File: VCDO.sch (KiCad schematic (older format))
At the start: 84 parts, among them J1 PCB INTERCONNECT, J2 PROGRAMMING HEADER, Q1 2N3904, U1 TL074, U2 Druid VCDO, U3 TL074, U4 TL072

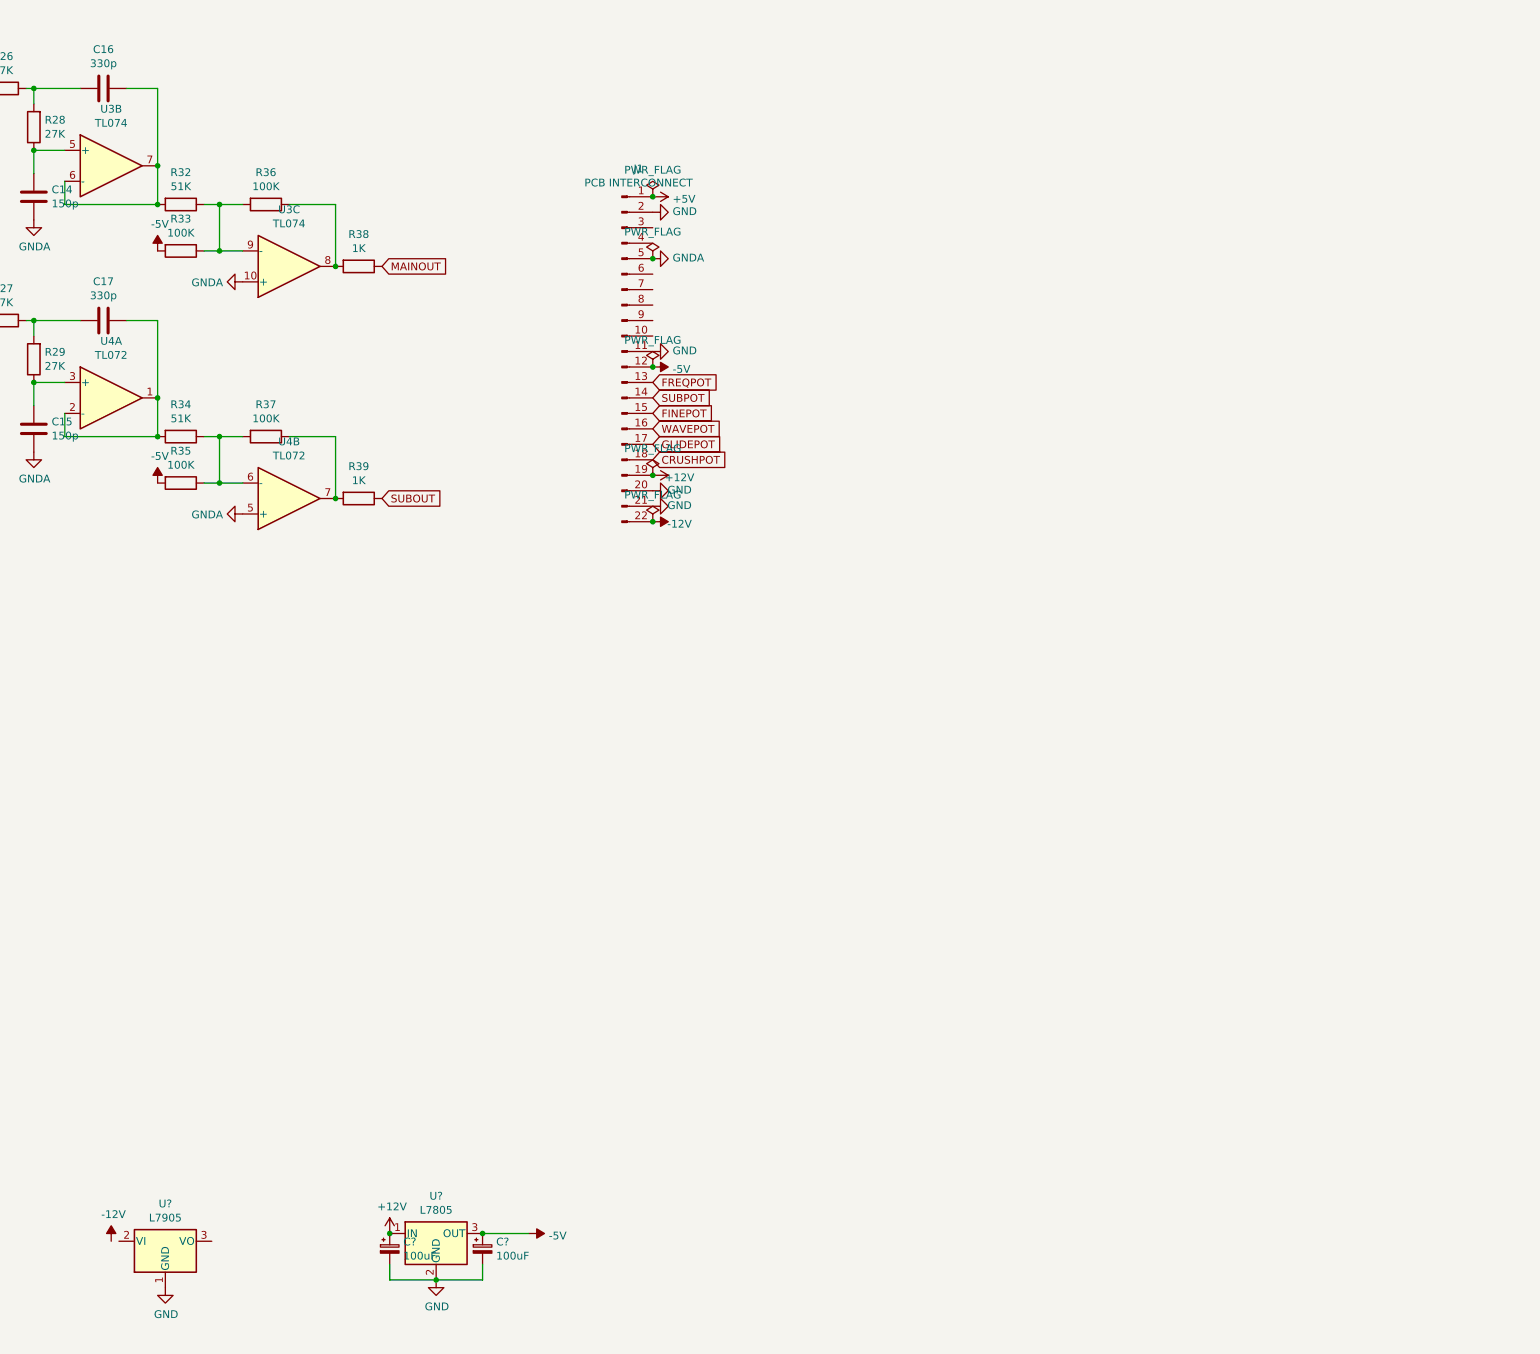
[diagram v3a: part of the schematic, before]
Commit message: no more conn, add pots
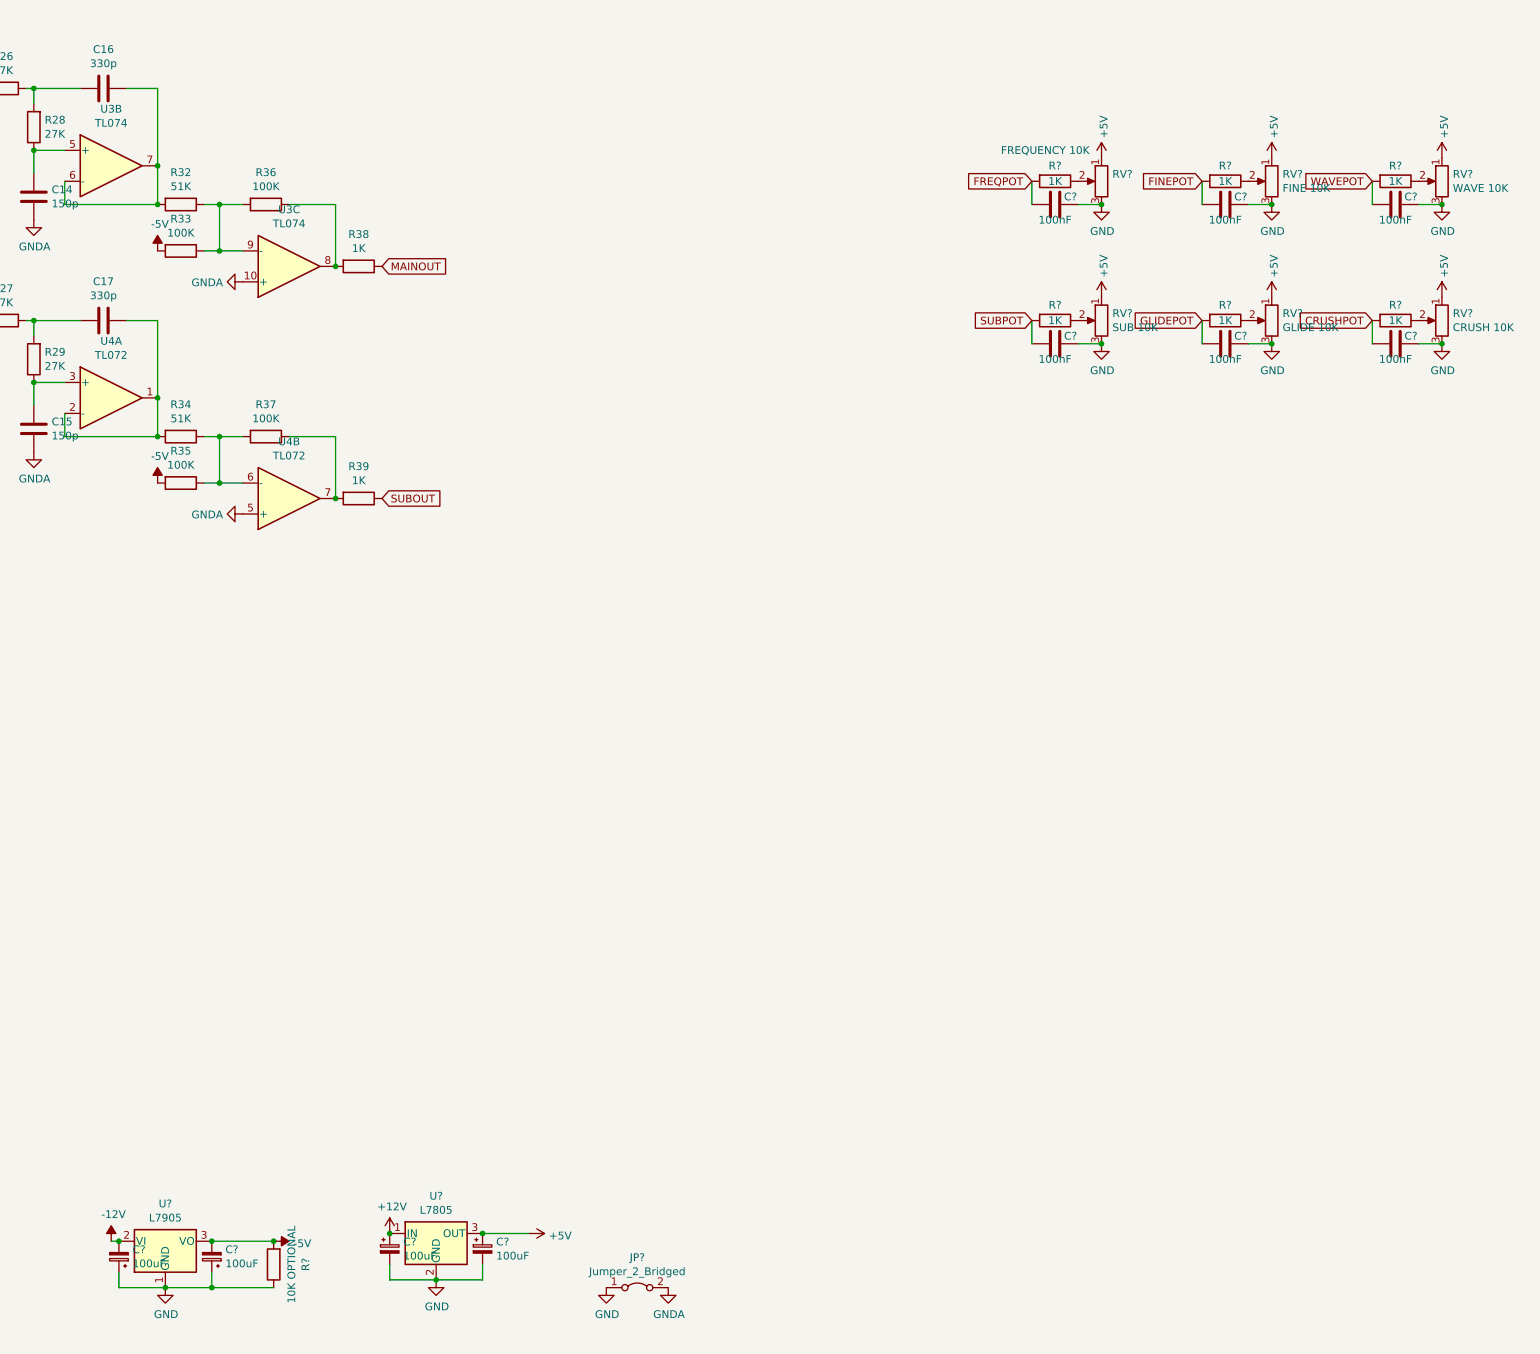
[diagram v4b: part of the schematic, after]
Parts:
- removed J1: PCB INTERCONNECT, Connector_PinHeader_2.54mm:PinHeader_1x22_P2.54mm_Vertical, symbol Connector:Conn_01x22_Male
- added C? (x2): 100uF, symbol Device:CP_Small
- added C? (x6): 100nF, symbol Device:C
- added JP?: Jumper_2_Bridged, symbol Jumper:Jumper_2_Bridged
- added R?: 10K OPTIONAL, Resistor_THT:R_Axial_DIN0207_L6.3mm_D2.5mm_P7.62mm_Horizontal, symbol Device:R
- added R? (x6): 1K, Resistor_THT:R_Axial_DIN0207_L6.3mm_D2.5mm_P7.62mm_Horizontal, symbol Device:R
- added RV?: FREQUENCY 10K, symbol Device:R_POT
- added RV?: FINE 10K, symbol Device:R_POT
- added RV?: WAVE 10K, symbol Device:R_POT
- added RV?: SUB 10K, symbol Device:R_POT
- added RV?: GLIDE 10K, symbol Device:R_POT
- added RV?: CRUSH 10K, symbol Device:R_POT
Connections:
- net +5V: now also C?.1, U?.3 (OUT), RV?.1, RV?.1, RV?.1, RV?.1, RV?.1, RV?.1
- net -12V: now also U?.2 (VI), C?.2
- net -5V: now also U?.3 (VO), C?.2, R?.2; no longer C?.1, U?.3 (OUT)
- net CRUSHPOT: now also C?.2, R?.2
- net FINEPOT: now also C?.2, R?.2
- net FREQPOT: now also C?.2, R?.2
- net GLIDEPOT: now also C?.2, R?.2
- net GND: now also C?.1, C?.1, C?.1, C?.1, C?.1, C?.1, C?.1, C?.1, JP?.1 (A), R?.1, RV?.3, RV?.3, RV?.3, RV?.3, RV?.3, RV?.3
- net GNDA: now also JP?.2 (B)
- net SUBPOT: now also C?.2, R?.2
- net WAVEPOT: now also C?.2, R?.2
- new net: R?.1, RV?.2 (x6)

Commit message: reannotate
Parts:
- gave numbers to parts that had none: 38
- renumbered C2 to C1, C11 to C10, C14 to C11, C15 to C12, C16 to C13, C17 to C14, C1 to C18, C3 to C2, C4 to C3, C5 to C4, C6 to C5, C7 to C6, C8 to C7, C9 to C8, C10 to C9, J2 to J10, R20 to R18, R21 to R19, R18 to R20, R22 to R21, R23 to R22, R26 to R23, R27 to R24, R28 to R25, R29 to R26, R32 to R27, R33 to R28, R34 to R29, R35 to R30, R36 to R31, R37 to R32, R38 to R34, R39 to R35, R19 to R36, RV1 to RV4, RV2 to RV5, RV3 to RV6, U3 to U2, U4 to U3, U2 to U6

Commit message: pwr flags
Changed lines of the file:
@@
 Wire Wire Line
 	14750 4600 14750 4750
+$Comp
+L power:PWR_FLAG #FLG0101
+U 1 1 60C07709
+P 4500 10000
+F 0 "#FLG0101" H 4500 10075 50  0001 C CNN
+F 1 "PWR_FLAG" H 4500 10173 50  0000 C CNN
+F 2 "" H 4500 10000 50  0001 C CNN
+F 3 "~" H 4500 10000 50  0001 C CNN
+	1    4500 10000
+	1    0    0    -1
+$EndComp
+Connection ~ 4500 10000
+$Comp
+L power:PWR_FLAG #FLG0102
+U 1 1 60C07B37
+P 4600 10400
+F 0 "#FLG0102" H 4600 10475 50  0001 C CNN
+F 1 "PWR_FLAG" H 4600 10573 50  0000 C CNN
+F 2 "" H 4600 10400 50  0001 C CNN
+F 3 "~" H 4600 10400 50  0001 C CNN
+	1    4600 10400
+	1    0    0    -1
+$EndComp
+Connection ~ 4600 10400
+$Comp
+L power:PWR_FLAG #FLG0103
+U 1 1 60C07EDA
+P 4000 10700
+F 0 "#FLG0103" H 4000 10775 50  0001 C CNN
+F 1 "PWR_FLAG" V 4000 10827 50  0000 L CNN
+F 2 "" H 4000 10700 50  0001 C CNN
+F 3 "~" H 4000 10700 50  0001 C CNN
+	1    4000 10700
+	0    -1   -1   0
+$EndComp
+Connection ~ 4000 10700
 $EndSCHEMATC

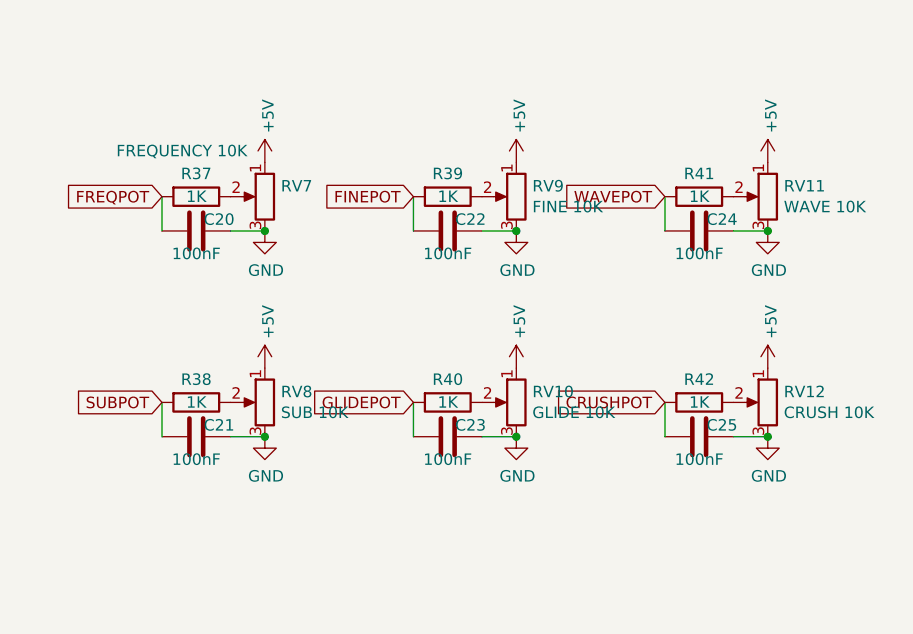
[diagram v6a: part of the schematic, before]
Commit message: no more resistors or caps on pots
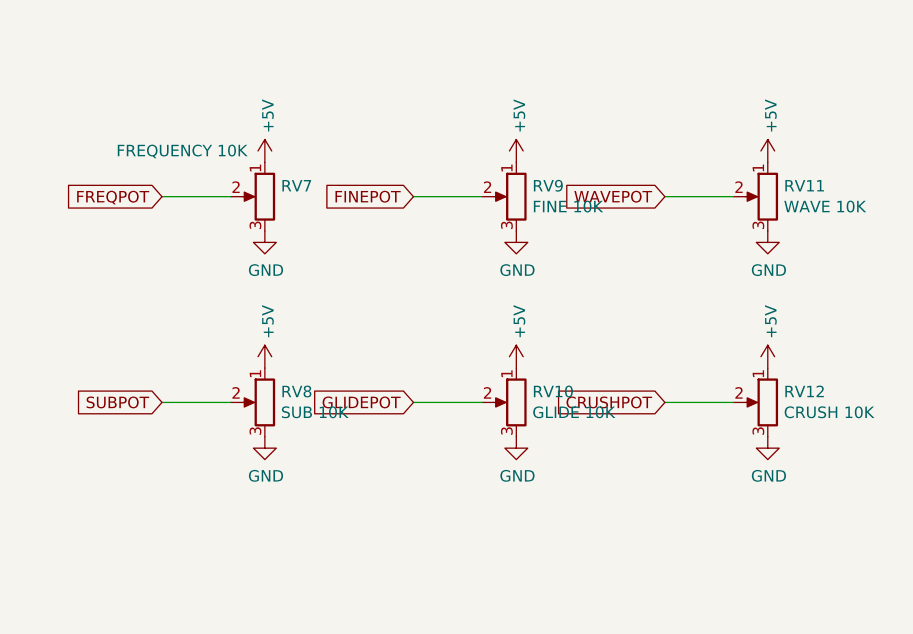
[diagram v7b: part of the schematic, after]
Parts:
- removed C20, C21, C22, C23, C24, C25: 100nF, symbol Device:C
- removed R37, R38, R39, R40, R41, R42: 1K, Resistor_THT:R_Axial_DIN0207_L6.3mm_D2.5mm_P7.62mm_Horizontal, symbol Device:R
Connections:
- net CRUSHPOT: now also RV12.2
- net FINEPOT: now also RV9.2
- net FREQPOT: now also RV7.2
- net GLIDEPOT: now also RV10.2
- net SUBPOT: now also RV8.2
- net WAVEPOT: now also RV11.2
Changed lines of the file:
@@
-$EndComp
-$Comp
-L Device:R R37
-U 1 1 60C8DA64
-P 12700 3700
-F 0 "R37" V 12600 3700 50  0000 C CNN
-F 1 "1K" V 12700 3700 50  0000 C CNN
-F 2 "Resistor_THT:R_Axial_DIN0207_L6.3mm_D2.5mm_P7.62mm_Horizontal" V 12630 3700 50  0001 C CNN
-F 3 "~" H 12700 3700 50  0001 C CNN
-	1    12700 3700
-	0    1    1    0
-$EndComp
-$Comp
-L Device:C C20
-U 1 1 60C945AD
-P 12700 3850
-F 0 "C20" V 12650 3950 50  0000 C CNN
-F 1 "100nF" V 12800 3850 50  0000 C CNN
-F 2 "" H 12738 3700 50  0001 C CNN
-F 3 "~" H 12700 3850 50  0001 C CNN
-	1    12700 3850
-	0    1    1    0
 $EndComp
 $Comp
@@
 	1    0    0    -1
 $EndComp
-Wire Wire Line
-	12850 3850 13000 3850
-Connection ~ 13000 3850
-Wire Wire Line
-	12550 3700 12550 3850
 $Comp
 L Device:R_POT RV9
@@
 $EndComp
 $Comp
-L Device:R R39
-U 1 1 60CA3A2C
-P 13800 3700
-F 0 "R39" V 13700 3700 50  0000 C CNN
-F 1 "1K" V 13800 3700 50  0000 C CNN
-F 2 "Resistor_THT:R_Axial_DIN0207_L6.3mm_D2.5mm_P7.62mm_Horizontal" V 13730 3700 50  0001 C CNN
-F 3 "~" H 13800 3700 50  0001 C CNN
-	1    13800 3700
-	0    1    1    0
-$EndComp
-$Comp
-L Device:C C22
-U 1 1 60CA3A36
-P 13800 3850
-F 0 "C22" V 13750 3950 50  0000 C CNN
-F 1 "100nF" V 13900 3850 50  0000 C CNN
-F 2 "" H 13838 3700 50  0001 C CNN
-F 3 "~" H 13800 3850 50  0001 C CNN
-	1    13800 3850
-	0    1    1    0
-$EndComp
-$Comp
 L power:+5V #PWR074
 U 1 1 60CA3A40
@@
 	1    0    0    -1
 $EndComp
-Wire Wire Line
-	13950 3850 14100 3850
-Connection ~ 14100 3850
-Wire Wire Line
-	13650 3700 13650 3850
 $Comp
 L Device:R_POT RV11
@@
 $EndComp
 $Comp
-L Device:R R41
-U 1 1 60CAB3F1
-P 14900 3700
-F 0 "R41" V 14800 3700 50  0000 C CNN
-F 1 "1K" V 14900 3700 50  0000 C CNN
-F 2 "Resistor_THT:R_Axial_DIN0207_L6.3mm_D2.5mm_P7.62mm_Horizontal" V 14830 3700 50  0001 C CNN
-F 3 "~" H 14900 3700 50  0001 C CNN
-	1    14900 3700
-	0    1    1    0
-$EndComp
-$Comp
-L Device:C C24
-U 1 1 60CAB3FB
-P 14900 3850
-F 0 "C24" V 14850 3950 50  0000 C CNN
-F 1 "100nF" V 15000 3850 50  0000 C CNN
-F 2 "" H 14938 3700 50  0001 C CNN
-F 3 "~" H 14900 3850 50  0001 C CNN
-	1    14900 3850
-	0    1    1    0
-$EndComp
-$Comp
 L power:+5V #PWR078
 U 1 1 60CAB405
@@
 	1    0    0    -1
 $EndComp
-Wire Wire Line
-	15050 3850 15200 3850
-Connection ~ 15200 3850
-Wire Wire Line
-	14750 3700 14750 3850
 $Comp
 L Device:R_POT RV8
@@
 $EndComp
 $Comp
-L Device:R R38
-U 1 1 60CB31F0
-P 12700 4600
-F 0 "R38" V 12600 4600 50  0000 C CNN
-F 1 "1K" V 12700 4600 50  0000 C CNN
-F 2 "Resistor_THT:R_Axial_DIN0207_L6.3mm_D2.5mm_P7.62mm_Horizontal" V 12630 4600 50  0001 C CNN
-F 3 "~" H 12700 4600 50  0001 C CNN
-	1    12700 4600
-	0    1    1    0
-$EndComp
-$Comp
-L Device:C C21
-U 1 1 60CB31FA
-P 12700 4750
-F 0 "C21" V 12650 4850 50  0000 C CNN
-F 1 "100nF" V 12800 4750 50  0000 C CNN
-F 2 "" H 12738 4600 50  0001 C CNN
-F 3 "~" H 12700 4750 50  0001 C CNN
-	1    12700 4750
-	0    1    1    0
-$EndComp
-$Comp
 L power:+5V #PWR072
 U 1 1 60CB3204
@@
 	1    0    0    -1
 $EndComp
-Wire Wire Line
-	12850 4750 13000 4750
-Connection ~ 13000 4750
-Wire Wire Line
-	12550 4600 12550 4750
 $Comp
 L Device:R_POT RV10
@@
 $EndComp
 $Comp
-L Device:R R40
-U 1 1 60CB3225
-P 13800 4600
-F 0 "R40" V 13700 4600 50  0000 C CNN
-F 1 "1K" V 13800 4600 50  0000 C CNN
-F 2 "Resistor_THT:R_Axial_DIN0207_L6.3mm_D2.5mm_P7.62mm_Horizontal" V 13730 4600 50  0001 C CNN
-F 3 "~" H 13800 4600 50  0001 C CNN
-	1    13800 4600
-	0    1    1    0
-$EndComp
-$Comp
-L Device:C C23
-U 1 1 60CB322F
-P 13800 4750
-F 0 "C23" V 13750 4850 50  0000 C CNN
-F 1 "100nF" V 13900 4750 50  0000 C CNN
-F 2 "" H 13838 4600 50  0001 C CNN
-F 3 "~" H 13800 4750 50  0001 C CNN
-	1    13800 4750
-	0    1    1    0
-$EndComp
-$Comp
 L power:+5V #PWR076
 U 1 1 60CB3239
@@
 	1    0    0    -1
 $EndComp
-Wire Wire Line
-	13950 4750 14100 4750
-Connection ~ 14100 4750
-Wire Wire Line
-	13650 4600 13650 4750
-$Comp
-L Device:R_POT RV12
-U 1 1 60CB3250
-P 15200 4600
-F 0 "RV12" H 15130 4646 50  0000 R CNN
-F 1 "CRUSH 10K" H 15130 4555 50  0000 R CNN
-F 2 "" H 15200 4600 50  0001 C CNN
-F 3 "~" H 15200 4600 50  0001 C CNN
-	1    15200 4600
-	-1   0    0    -1
-$EndComp
-$Comp
-L Device:R R42
-U 1 1 60CB325A
-P 14900 4600
-F 0 "R42" V 14800 4600 50  0000 C CNN
-F 1 "1K" V 14900 4600 50  0000 C CNN
-F 2 "Resistor_THT:R_Axial_DIN0207_L6.3mm_D2.5mm_P7.62mm_Horizontal" V 14830 4600 50  0001 C CNN
-F 3 "~" H 14900 4600 50  0001 C CNN
-	1    14900 4600
-	0    1    1    0
-$EndComp
-$Comp
-L Device:C C25
-U 1 1 60CB3264
-P 14900 4750
-F 0 "C25" V 14850 4850 50  0000 C CNN
-F 1 "100nF" V 15000 4750 50  0000 C CNN
-F 2 "" H 14938 4600 50  0001 C CNN
-F 3 "~" H 14900 4750 50  0001 C CNN
-	1    14900 4750
-	0    1    1    0
-$EndComp
 $Comp
 L power:+5V #PWR080
@@
 	1    0    0    -1
 $EndComp
-Wire Wire Line
-	15050 4750 15200 4750
-Connection ~ 15200 4750
-Wire Wire Line
-	14750 4600 14750 4750
 $Comp
 L power:PWR_FLAG #FLG0101
@@
 $EndComp
 Connection ~ 4000 10700
+$Comp
+L Device:R_POT RV12
+U 1 1 60CB3250
+P 15200 4600
+F 0 "RV12" H 15130 4646 50  0000 R CNN
+F 1 "CRUSH 10K" H 15130 4555 50  0000 R CNN
+F 2 "" H 15200 4600 50  0001 C CNN
+F 3 "~" H 15200 4600 50  0001 C CNN
+	1    15200 4600
+	-1   0    0    -1
+$EndComp
+Wire Wire Line
+	15050 3700 14750 3700
+Wire Wire Line
+	13950 3700 13650 3700
+Wire Wire Line
+	12850 3700 12550 3700
+Wire Wire Line
+	12850 4600 12550 4600
+Wire Wire Line
+	13950 4600 13650 4600
+Wire Wire Line
+	15050 4600 14750 4600
 $EndSCHEMATC

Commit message: fooootprints
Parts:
- C1, C10, C11, C12, C13, C14, C18, C2, C3, C4, C5, C6, C7, C8, C9: footprint Capacitor_THT:C_Disc_D6.0mm_W4.4mm_P5.00mm -> Sonosus:Capacitor_NonPolarized
- C15, C16, C17, C19: footprint (none) -> Sonosus:Capacitor_Polarized
- D1, D2, D3, D4, D5, D6, D7, D8: footprint Diode_THT:D_DO-35_SOD27_P7.62mm_Horizontal -> Sonosus:Diode_DO-35
- J1, J2, J3, J4, J5, J6, J9: footprint (none) -> Connector_PinHeader_2.54mm:PinHeader_1x02_P2.54mm_Vertical
- J7: footprint (none) -> Connector_PinHeader_2.54mm:PinHeader_1x03_P2.54mm_Vertical
- J8: footprint (none) -> Connector_PinHeader_2.54mm:PinHeader_2x05_P2.54mm_Vertical
- JP1: footprint (none) -> Jumper:SolderJumper-2_P1.3mm_Bridged2Bar_Pad1.0x1.5mm
- Q1: footprint Package_TO_SOT_THT:TO-92_Inline -> Sonosus:Transistor_TO-92
- R1, R10, R11, R12, R13, R14, R15, R16, R17, R18, R19, R2, R20, R21, R22, R23, R24, R25, R26, R27, R28, R29, R3, R30, R31, R32, R33, R34, R35, R36, R4, R5, R6, R7, R8, R9: footprint Resistor_THT:R_Axial_DIN0207_L6.3mm_D2.5mm_P7.62mm_Horizontal -> Sonosus:Resistor
- RV1, RV2, RV3: footprint Potentiometer_THT:Potentiometer_Bourns_3296W_Vertical -> Sonosus:Potentiometer_Alpha_RD901F-40-00D
- RV10, RV11, RV12, RV7, RV8, RV9: footprint (none) -> Sonosus:Potentiometer_Alpha_RD901F-40-00D
- U1, U2: footprint Package_DIP:DIP-14_W7.62mm_Socket_LongPads -> Sonosus:DIP-14_Socket
- U3: footprint Package_DIP:DIP-8_W7.62mm_Socket_LongPads -> Sonosus:DIP-8_Socket
- U4, U5: footprint (none) -> Package_TO_SOT_THT:TO-220-3_Vertical
